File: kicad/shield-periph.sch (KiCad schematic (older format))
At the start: 6 parts, among them J4 Fix, J5 Fix, J6 Fix, J7 Fix, U2 Shield_droite, U3 Shield_gauche

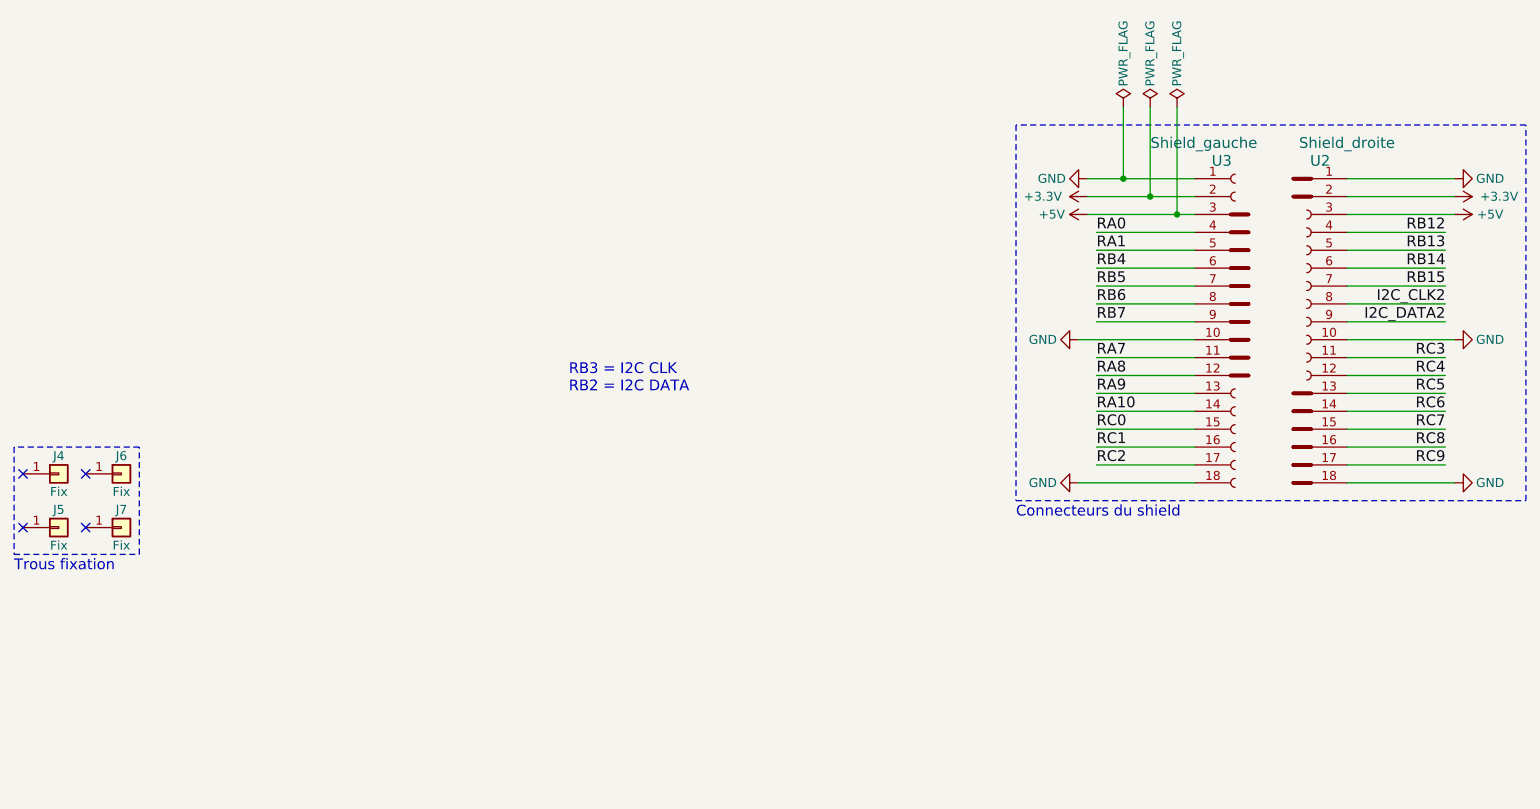
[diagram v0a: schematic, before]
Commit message: Création empreinte connecteur unique et mise à jour
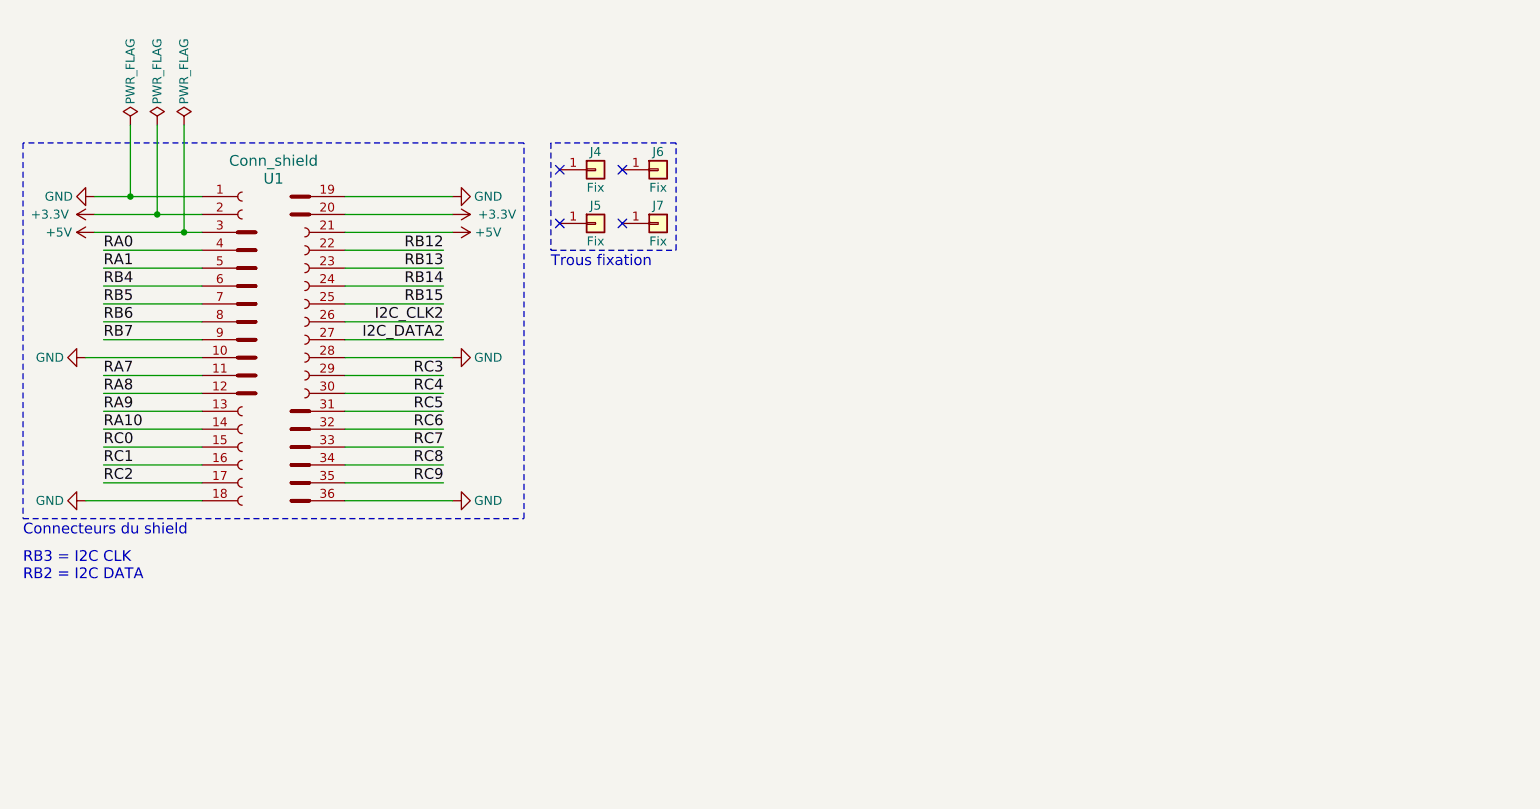
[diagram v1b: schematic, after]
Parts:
- removed U2: Shield_droite, conn_shield:conn_shield, symbol Conn_shield_1
- removed U3: Shield_gauche, conn_shield:conn_shield, symbol Conn_shield_2
- added U1: Conn_shield, conn_shield:conn_shield, symbol Conn_shield
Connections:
- net +3V3: now also U1.2, U1.20
- net +5V: now also U1.21, U1.3
- net GND: now also U1.1, U1.10, U1.18, U1.19, U1.28, U1.36
- net I2C_CLK2: now also U1.26
- net I2C_DATA2: now also U1.27
- net RA0: now also U1.4
- net RA1: now also U1.5
- net RA10: now also U1.14
- net RA7: now also U1.11
- net RA8: now also U1.12
- net RA9: now also U1.13
- net RB12: now also U1.22
- net RB13: now also U1.23
- net RB14: now also U1.24
- net RB15: now also U1.25
- net RB4: now also U1.6
- net RB5: now also U1.7
- net RB6: now also U1.8
- net RB7: now also U1.9
- net RC0: now also U1.15
- net RC1: now also U1.16
- net RC2: now also U1.17
- net RC3: now also U1.29
- net RC4: now also U1.30
- net RC5: now also U1.31
- net RC6: now also U1.32
- net RC7: now also U1.33
- net RC8: now also U1.34
- net RC9: now also U1.35
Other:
- moved on the sheet: J4, J5, J6, J7

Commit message: Mise en conformité avec la carte periph
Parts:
- removed J4, J5, J6, J7: Fix, Mounting_Holes:MountingHole_3.2mm_M3_Pad, symbol Conn_01x01
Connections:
- net labels removed: I2C_CLK2, I2C_DATA2, RA0, RA1, RA10, RA7, RA8, RA9, RB12, RB13, RB14, RB15, RB4, RB5, RB6, RB7, RC0, RC1, RC2, RC3, RC4, RC5, RC6, RC7, RC8, RC9
- wire segments 39 -> 16
- no-connect marks 4 -> 0
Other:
- note added: "Relier L1 et V34 si \nbesoin d'un PIC 44 pattes"
- note removed: "Trous fixation"
